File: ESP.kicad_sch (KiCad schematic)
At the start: 25 parts, among them J11 USB_C_Receptacle_USB2.0_16P, J12 UART_Breakout, U1 TLV1117LV33DCYR, U3 ESP32-C6-MINI-1/U

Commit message: is it time to give up :3
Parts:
- removed D6, D7: TVS, Diode_SMD:D_0603_1608Metric, symbol Device:D_TVS
- added D5: PRTR5V0U2AX,215, tv diode:PRTR5V0U2X, symbol tvs diode:PRTR5V0U2AX,215
- C10: renamed from C9; footprint Capacitor_SMD:C_0603_1608Metric -> Capacitor_SMD:C_0805_2012Metric
- C11: renamed from C10; footprint Capacitor_SMD:C_0603_1608Metric -> Capacitor_SMD:C_0805_2012Metric
- C4: renamed from C3; footprint Capacitor_SMD:C_0603_1608Metric -> Capacitor_SMD:C_0805_2012Metric
- C5: renamed from C4; footprint Capacitor_SMD:C_0603_1608Metric -> Capacitor_SMD:C_0805_2012Metric
- C6: renamed from C5; footprint Capacitor_SMD:C_0603_1608Metric -> Capacitor_SMD:C_0805_2012Metric
- C8: renamed from C7; footprint Capacitor_SMD:C_0603_1608Metric -> Capacitor_SMD:C_0805_2012Metric
- D2, D3: footprint LED_SMD:LED_0603_1608Metric -> LED_SMD:LED_0805_2012Metric
- renumbered C6 to C7, C8 to C9, D5 to D6, J11 to J10, J12 to J11
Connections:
- net BOOT: now also U3.24 (GPIO18); no longer U3.23 (GPIO9)
- net GND: now also D5.1 (GND)
- net LED3: now also U3.23 (GPIO9); no longer U3.24 (GPIO18)
- net USB_D+: now also D5.3 (IO2)
- net USB_D-: now also D5.2 (IO1)
- net VBUSB: now also D5.4 (VIN)
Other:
- moved on the sheet: C11, D6, R13, R14

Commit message: minor fixes
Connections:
- net BOOT: now also U3.25 (GPIO19); no longer U3.24 (GPIO18)
- net LED4: now also U3.24 (GPIO18); no longer U3.25 (GPIO19)
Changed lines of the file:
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@@
 		)
 	)
+	(label "BOOT"
+		(at 213.36 76.2 180)
+		(effects
+			(font
+				(size 1.27 1.27)
+			)
+			(justify right bottom)
+		)
+	)
 	(label "3V3_USB"
 		(at 41.91 43.18 0)
@@
 		)
 	)
-	(label "3V3"
-		(at 118.11 43.18 180)
+	(label "LED4"
+		(at 213.36 73.66 180)
 		(effects
 			(font
@@
 		)
 	)
-	(label "LED4"
-		(at 213.36 76.2 180)
+	(label "3V3"
+		(at 118.11 43.18 180)
 		(effects
 			(font
@@
 		)
 	)
-	(label "BOOT"
-		(at 213.36 73.66 180)
-		(effects
-			(font
-				(size 1.27 1.27)
-			)
-			(justify right bottom)
-		)
-	)
 	(label "IO6"
 		(at 281.305 71.755 180)
@@
 		(dnp no)
 		(fields_autoplaced yes)
-		(property "Reference" "#PWR044"
+		(property "Reference" "#PWR043"
 			(at 175.26 104.14 0)
 			(effects
@@
 			(project ""
 				(path "/795c8e51-3ded-4d21-b864-aaff31c5def7/6282503b-e4ab-454b-a074-f701a067f39b"
-					(reference "#PWR044")
+					(reference "#PWR043")
 					(unit 1)
 				)
@@
 			)
 		)
-		(property "Datasheet" ""
+		(property "Datasheet" "https://www.ti.com/lit/ds/symlink/lm66200.pdf?ts=1749979530840&ref_url=https%253A%252F%252Fwww.ti.com%252Fproduct%252FLM66200%253Futm_source%253Dgoogle%2526utm_medium%253Dcpc%2526utm_campaign%253Dapp-psil-null-44700045336317533_prodfolderdynamic-cpc-pf-google-eu_en_int%2526utm_content%253Dprodfolddynamic%2526ds_k%253DDYNAMIC+SEARCH+ADS%2526DCM%253Dyes%2526gad_source%253D1%2526gad_campaignid%253D8846228537%2526gbraid%253D0AAAAAC068F1nk_tvmYl3HXqK31USHPiW6%2526gclid%253DCjwKCAjw3rnCBhBxEiwArN0QE3nkB2-V_-iCZj5EyJCU-GAaAYaAjT6NO-eVHse-p8kje0rPcw2oyxoCwP4QAvD_BwE%2526gclsrc%253Daw.ds"
 			(at 77.47 44.45 0)
 			(effects
@@
 		(dnp no)
 		(fields_autoplaced yes)
-		(property "Reference" "#PWR043"
+		(property "Reference" "#PWR044"
 			(at 178.435 165.735 0)
 			(effects
@@
 			(project "VehicleControlUnit"
 				(path "/795c8e51-3ded-4d21-b864-aaff31c5def7/6282503b-e4ab-454b-a074-f701a067f39b"
-					(reference "#PWR043")
+					(reference "#PWR044")
 					(unit 1)
 				)
@@
 			)
 		)
-		(property "Datasheet" "~"
+		(property "Datasheet" "https://www.mouser.com/datasheet/2/80/CPDxx5V0R_HF_Series_RevC661473-2505247.pdf"
 			(at 201.295 146.05 0)
 			(effects

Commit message: 24v changes
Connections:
- net BOOT: now also U3.24 (GPIO18); no longer U3.25 (GPIO19)
- net LED3: now also U3.22 (GPIO8); no longer U3.23 (GPIO9)
- net LED4: now also U3.23 (GPIO9); no longer U3.24 (GPIO18)
- no-connect marks 3 -> 2
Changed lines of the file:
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@@
-	)
-	(no_connect
-		(at 203.2 63.5)
 	)
 	(no_connect
@@
 	(wire
 		(pts
+			(xy 203.2 66.04) (xy 213.36 66.04)
+		)
+		(stroke
+			(width 0)
+			(type default)
+		)
+	)
+	(wire
+		(pts
 			(xy 93.98 43.18) (xy 106.68 43.18)
 		)
@@
 	(wire
 		(pts
-			(xy 203.2 66.04) (xy 213.36 66.04)
-		)
-		(stroke
-			(width 0)
-			(type default)
-		)
-	)
-	(wire
-		(pts
 			(xy 213.36 45.72) (xy 219.71 45.72)
 		)
@@
 	(wire
 		(pts
+			(xy 203.2 73.66) (xy 213.36 73.66)
+		)
+		(stroke
+			(width 0)
+			(type default)
+		)
+	)
+	(wire
+		(pts
 			(xy 116.84 167.64) (xy 116.84 170.18)
 		)
@@
 	(wire
 		(pts
-			(xy 203.2 73.66) (xy 213.36 73.66)
-		)
-		(stroke
-			(width 0)
-			(type default)
-		)
-	)
-	(wire
-		(pts
 			(xy 203.2 43.18) (xy 210.82 43.18)
 		)
@@
 	(wire
 		(pts
+			(xy 203.2 63.5) (xy 213.36 63.5)
+		)
+		(stroke
+			(width 0)
+			(type default)
+		)
+	)
+	(wire
+		(pts
 			(xy 142.24 149.86) (xy 151.13 149.86)
 		)
@@
 		(pts
 			(xy 139.7 149.86) (xy 142.24 149.86)
-		)
-		(stroke
-			(width 0)
-			(type default)
-		)
-	)
-	(wire
-		(pts
-			(xy 203.2 76.2) (xy 213.36 76.2)
 		)
 		(stroke
@@
 		)
 	)
-	(label "LED3"
-		(at 213.36 66.04 180)
-		(effects
-			(font
-				(size 1.27 1.27)
-			)
-			(justify right bottom)
-		)
-	)
 	(label "IO3"
 		(at 230.505 88.265 0)
@@
 		)
 	)
-	(label "BOOT"
-		(at 213.36 76.2 180)
-		(effects
-			(font
-				(size 1.27 1.27)
-			)
-			(justify right bottom)
-		)
-	)
 	(label "3V3_USB"
 		(at 41.91 43.18 0)
@@
 		)
 	)
+	(label "LED4"
+		(at 213.36 66.04 180)
+		(effects
+			(font
+				(size 1.27 1.27)
+			)
+			(justify right bottom)
+		)
+	)
 	(label "3V3"
 		(at 175.26 26.67 270)
@@
 		)
 	)
+	(label "LED3"
+		(at 213.36 63.5 180)
+		(effects
+			(font
+				(size 1.27 1.27)
+			)
+			(justify right bottom)
+		)
+	)
 	(label "LED1"
 		(at 213.36 68.58 180)
@@
 		)
 	)
-	(label "LED4"
-		(at 213.36 73.66 180)
-		(effects
-			(font
-				(size 1.27 1.27)
-			)
-			(justify right bottom)
-		)
-	)
 	(label "3V3"
 		(at 118.11 43.18 180)
@@
 		(effects
 			(font
+				(size 1.27 1.27)
+			)
+			(justify right bottom)
+		)
+	)
+	(label "BOOT"
+		(at 213.36 73.66 180)
+		(effects
+			(font

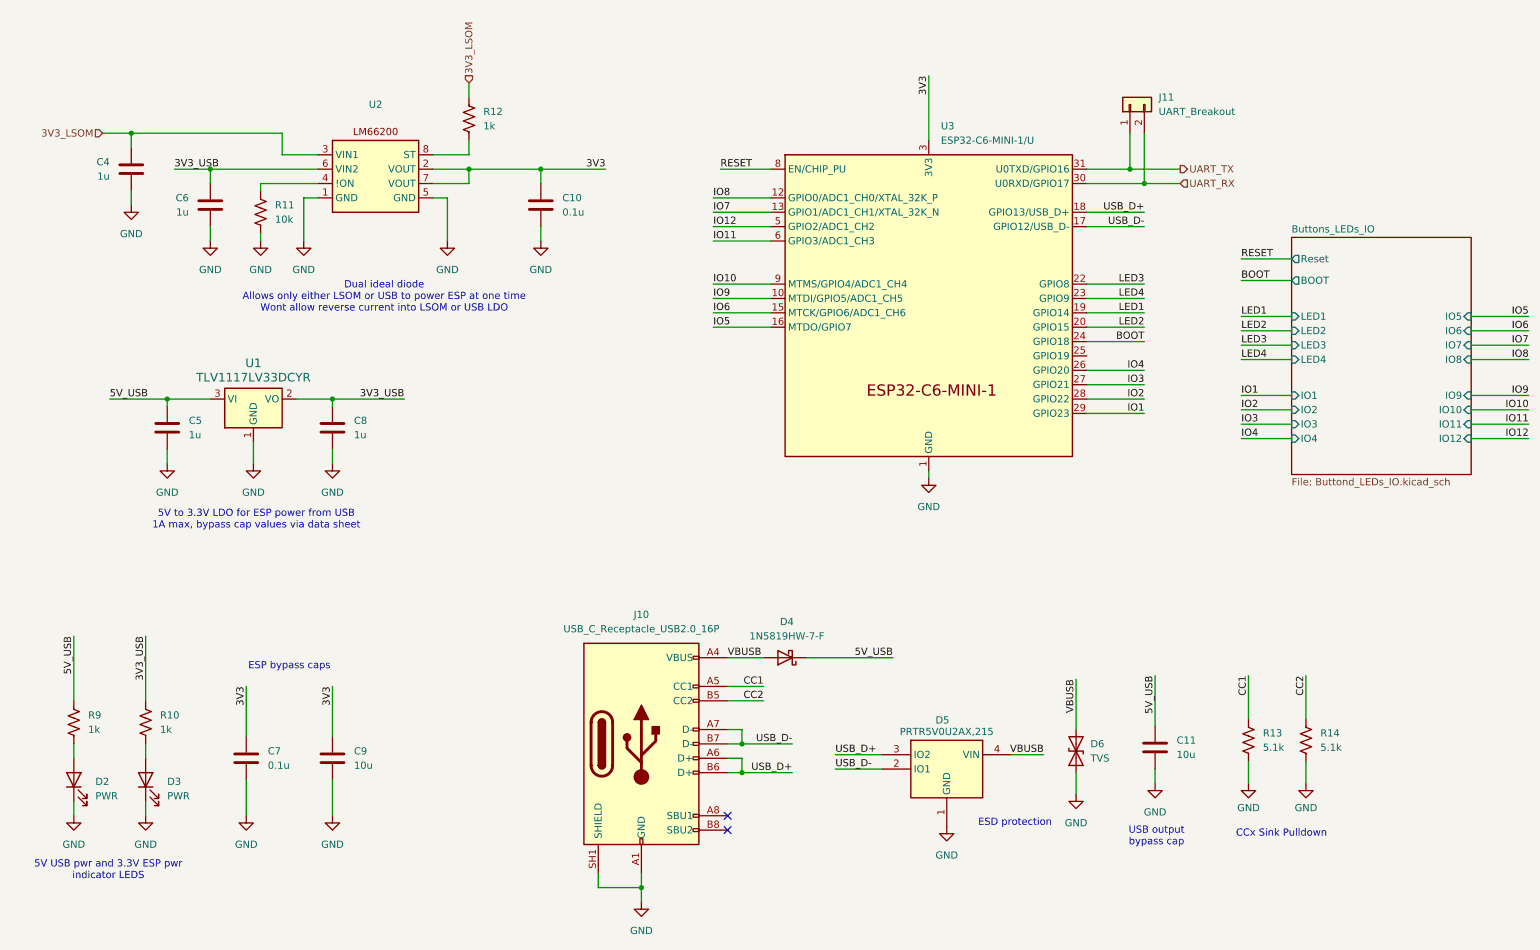
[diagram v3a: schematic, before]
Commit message: moving to kicad-bild
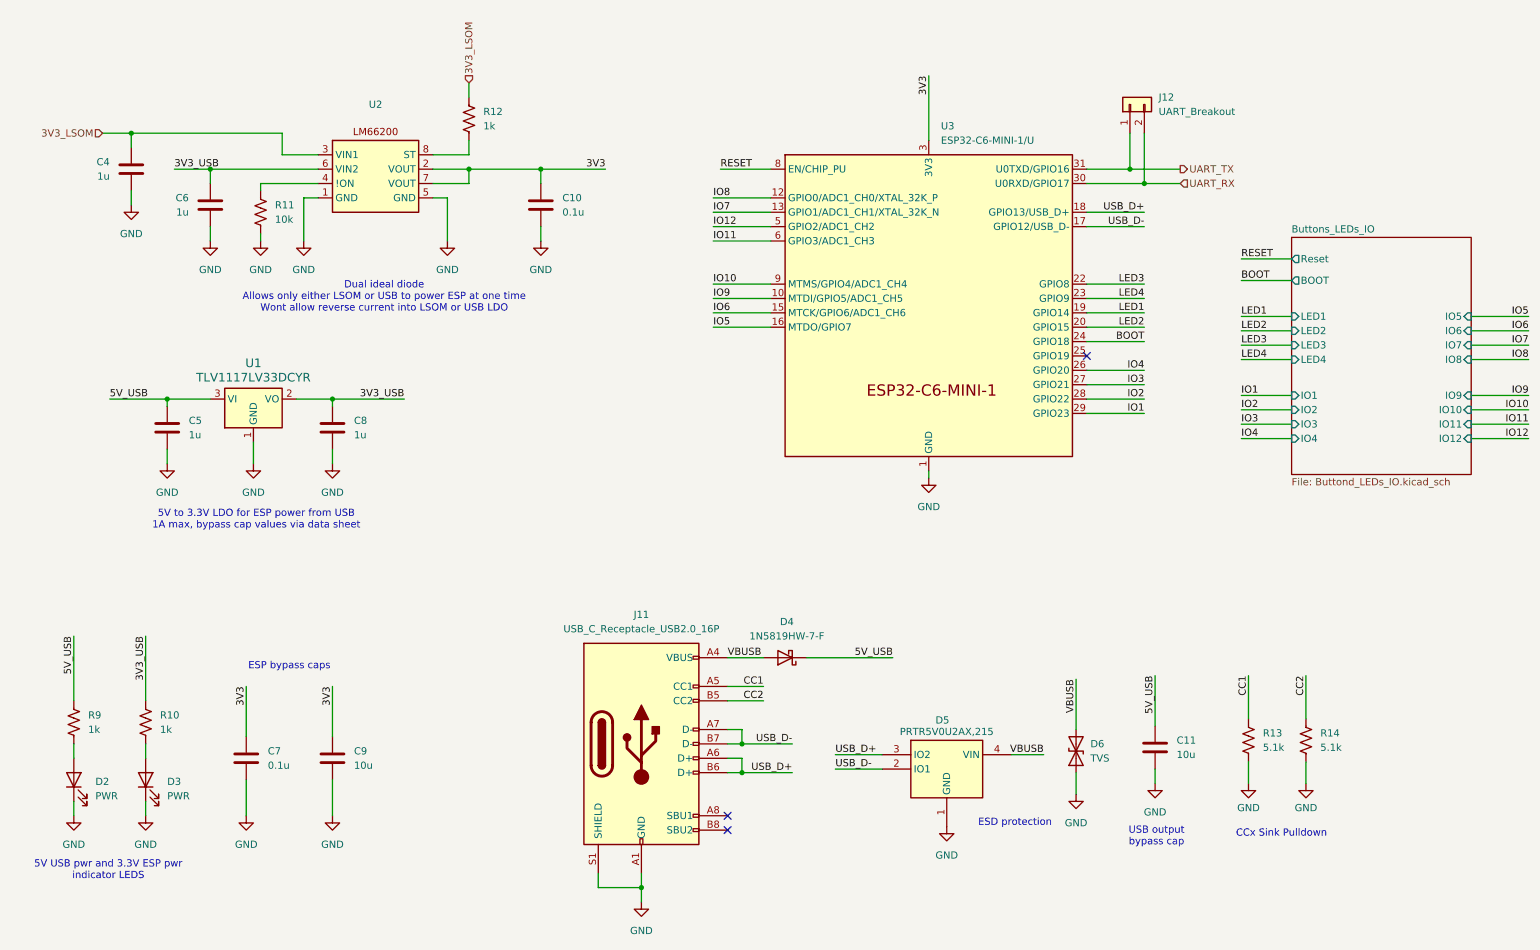
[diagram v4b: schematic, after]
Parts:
- renumbered J10 to J11, J11 to J12
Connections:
- net GND: now also J11.S1 (SHIELD); no longer J11.SH1 (SHIELD), J11.SH2 (SHIELD), J11.SH3 (SHIELD), J11.SH4 (SHIELD)
- no-connect marks 2 -> 3
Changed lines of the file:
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@@
 	)
 	(no_connect
+		(at 203.2 76.2)
+	)
+	(no_connect
 		(at 139.7 160.02)
 	)
@@
 		(dnp no)
 		(fields_autoplaced yes)
-		(property "Reference" "#PWR032"
+		(property "Reference" "#PWR034"
 			(at 40.64 101.6 0)
 			(effects
@@
 			(project "VehicleControlUnit"
 				(path "/795c8e51-3ded-4d21-b864-aaff31c5def7/6282503b-e4ab-454b-a074-f701a067f39b"
-					(reference "#PWR032")
+					(reference "#PWR034")
 					(unit 1)
 				)
@@
 		(on_board yes)
 		(dnp no)
-		(property "Reference" "#PWR047"
+		(property "Reference" "#PWR049"
 			(at 231.775 158.115 0)
 			(effects
@@
 			(project "VehicleControlUnit"
 				(path "/795c8e51-3ded-4d21-b864-aaff31c5def7/6282503b-e4ab-454b-a074-f701a067f39b"
-					(reference "#PWR047")
+					(reference "#PWR049")
 					(unit 1)
 				)
@@
 		(dnp no)
 		(fields_autoplaced yes)
-		(property "Reference" "#PWR037"
+		(property "Reference" "#PWR039"
 			(at 64.77 62.23 0)
 			(effects
@@
 			(project "VehicleControlUnit"
 				(path "/795c8e51-3ded-4d21-b864-aaff31c5def7/6282503b-e4ab-454b-a074-f701a067f39b"
-					(reference "#PWR037")
+					(reference "#PWR039")
 					(unit 1)
 				)
@@
 		(dnp no)
 		(fields_autoplaced yes)
-		(property "Reference" "#PWR038"
+		(property "Reference" "#PWR040"
 			(at 69.85 101.6 0)
 			(effects
@@
 			(project "VehicleControlUnit"
 				(path "/795c8e51-3ded-4d21-b864-aaff31c5def7/6282503b-e4ab-454b-a074-f701a067f39b"
-					(reference "#PWR038")
+					(reference "#PWR040")
 					(unit 1)
 				)
@@
 		(dnp no)
 		(fields_autoplaced yes)
-		(property "Reference" "#PWR031"
+		(property "Reference" "#PWR033"
 			(at 36.83 163.83 0)
 			(effects
@@
 			(project "VehicleControlUnit"
 				(path "/795c8e51-3ded-4d21-b864-aaff31c5def7/6282503b-e4ab-454b-a074-f701a067f39b"
-					(reference "#PWR031")
+					(reference "#PWR033")
 					(unit 1)
 				)
@@
 		(dnp no)
 		(fields_autoplaced yes)
-		(property "Reference" "#PWR033"
+		(property "Reference" "#PWR035"
 			(at 48.26 62.23 0)
 			(effects
@@
 			(project "VehicleControlUnit"
 				(path "/795c8e51-3ded-4d21-b864-aaff31c5def7/6282503b-e4ab-454b-a074-f701a067f39b"
-					(reference "#PWR033")
+					(reference "#PWR035")
 					(unit 1)
 				)
@@
 		(dnp no)
 		(fields_autoplaced yes)
-		(property "Reference" "J11"
+		(property "Reference" "J12"
 			(at 215.9 30.4799 90)
 			(effects
@@
 			(project ""
 				(path "/795c8e51-3ded-4d21-b864-aaff31c5def7/6282503b-e4ab-454b-a074-f701a067f39b"
-					(reference "J11")
+					(reference "J12")
 					(unit 1)
 				)
@@
 		(dnp no)
 		(fields_autoplaced yes)
-		(property "Reference" "#PWR043"
+		(property "Reference" "#PWR045"
 			(at 175.26 104.14 0)
 			(effects
@@
 			(project ""
 				(path "/795c8e51-3ded-4d21-b864-aaff31c5def7/6282503b-e4ab-454b-a074-f701a067f39b"
-					(reference "#PWR043")
+					(reference "#PWR045")
 					(unit 1)
 				)
@@
 		(dnp no)
 		(fields_autoplaced yes)
-		(property "Reference" "#PWR042"
+		(property "Reference" "#PWR044"
 			(at 124.46 179.07 0)
 			(effects
@@
 			(project "VehicleControlUnit"
 				(path "/795c8e51-3ded-4d21-b864-aaff31c5def7/6282503b-e4ab-454b-a074-f701a067f39b"
-					(reference "#PWR042")
+					(reference "#PWR044")
 					(unit 1)
 				)
@@
 			)
 		)
-		(property "Datasheet" "https://www.diodes.com/assets/Datasheets/1N5819HW.pdf"
+		(property "Datasheet" "~"
 			(at 149.86 129.54 0)
 			(effects
@@
 			)
 		)
+		(property "Sim.Pins" "1=K 2=A"
+			(at 36.83 151.13 0)
+			(effects
+				(font
+					(size 1.27 1.27)
+				)
+				(hide yes)
+			)
+		)
 		(pin "2"
 		)
@@
 		(dnp no)
 		(fields_autoplaced yes)
-		(property "Reference" "#PWR046"
+		(property "Reference" "#PWR048"
 			(at 215.265 158.115 0)
 			(effects
@@
 			(project "VehicleControlUnit"
 				(path "/795c8e51-3ded-4d21-b864-aaff31c5def7/6282503b-e4ab-454b-a074-f701a067f39b"
-					(reference "#PWR046")
+					(reference "#PWR048")
 					(unit 1)
 				)
@@
 			)
 		)
+		(property "Sim.Pins" "1=K 2=A"
+			(at 24.13 151.13 0)
+			(effects
+				(font
+					(size 1.27 1.27)
+				)
+				(hide yes)
+			)
+		)
 		(pin "2"
 		)
@@
 		(dnp no)
 		(fields_autoplaced yes)
-		(property "Reference" "J10"
+		(property "Reference" "J11"
 			(at 124.46 121.92 0)
 			(effects
@@
 			)
 		)
-		(property "Datasheet" "https://www.mouser.com/datasheet/2/837/usb4215-3472997.pdf"
+		(property "Datasheet" "https://www.usb.org/sites/default/files/documents/usb_type-c.zip"
 			(at 128.27 144.78 0)
 			(effects
@@
 		(pin "A1"
 		)
-		(pin "SH3"
-		)
 		(pin "B12"
 		)
@@
 		(pin "A8"
 		)
-		(pin "SH4"
-		)
-		(pin "SH2"
-		)
-		(pin "SH1"
+		(pin "S1"
 		)
 		(instances
 			(project "VehicleControlUnit"
 				(path "/795c8e51-3ded-4d21-b864-aaff31c5def7/6282503b-e4ab-454b-a074-f701a067f39b"
-					(reference "J10")
+					(reference "J11")
 					(unit 1)
 				)
@@
 		(dnp no)
 		(fields_autoplaced yes)
-		(property "Reference" "#PWR029"
+		(property "Reference" "#PWR031"
 			(at 24.13 163.83 0)
 			(effects
@@
 			(project "VehicleControlUnit"
 				(path "/795c8e51-3ded-4d21-b864-aaff31c5def7/6282503b-e4ab-454b-a074-f701a067f39b"
-					(reference "#PWR029")
+					(reference "#PWR031")
 					(unit 1)
 				)
@@
 		(dnp no)
 		(fields_autoplaced yes)
-		(property "Reference" "#PWR036"
+		(property "Reference" "#PWR038"
 			(at 57.15 62.23 0)
 			(effects
@@
 			(project "VehicleControlUnit"
 				(path "/795c8e51-3ded-4d21-b864-aaff31c5def7/6282503b-e4ab-454b-a074-f701a067f39b"
-					(reference "#PWR036")
+					(reference "#PWR038")
 					(unit 1)
 				)
@@
 		(dnp no)
 		(fields_autoplaced yes)
-		(property "Reference" "#PWR041"
+		(property "Reference" "#PWR043"
 			(at 106.68 62.23 0)
 			(effects
@@
 			(project "VehicleControlUnit"
 				(path "/795c8e51-3ded-4d21-b864-aaff31c5def7/6282503b-e4ab-454b-a074-f701a067f39b"
-					(reference "#PWR041")
+					(reference "#PWR043")
 					(unit 1)
 				)
@@
 	)
 	(symbol
-		(lib_name "R_US_1")
 		(lib_id "Device:R_US")
 		(at 231.775 144.145 0)
@@
 		(dnp no)
 		(fields_autoplaced yes)
-		(property "Reference" "#PWR035"
+		(property "Reference" "#PWR037"
 			(at 55.88 101.6 0)
 			(effects
@@
 			(project "VehicleControlUnit"
 				(path "/795c8e51-3ded-4d21-b864-aaff31c5def7/6282503b-e4ab-454b-a074-f701a067f39b"
-					(reference "#PWR035")
+					(reference "#PWR037")
 					(unit 1)
 				)
@@
 		(dnp no)
 		(fields_autoplaced yes)
-		(property "Reference" "#PWR045"
+		(property "Reference" "#PWR047"
 			(at 201.295 160.02 0)
 			(effects
@@
 			(project "VehicleControlUnit"
 				(path "/795c8e51-3ded-4d21-b864-aaff31c5def7/6282503b-e4ab-454b-a074-f701a067f39b"
-					(reference "#PWR045")
+					(reference "#PWR047")
 					(unit 1)
 				)
@@
 		(dnp no)
 		(fields_autoplaced yes)
-		(property "Reference" "#PWR039"
+		(property "Reference" "#PWR041"
 			(at 69.85 163.83 0)
 			(effects
@@
 			(project "VehicleControlUnit"
 				(path "/795c8e51-3ded-4d21-b864-aaff31c5def7/6282503b-e4ab-454b-a074-f701a067f39b"
-					(reference "#PWR039")
+					(reference "#PWR041")
 					(unit 1)
 				)
@@
 		(on_board yes)
 		(dnp no)
-		(property "Reference" "#PWR048"
+		(property "Reference" "#PWR050"
 			(at 241.935 158.115 0)
 			(effects
@@
 			(project "VehicleControlUnit"
 				(path "/795c8e51-3ded-4d21-b864-aaff31c5def7/6282503b-e4ab-454b-a074-f701a067f39b"
-					(reference "#PWR048")
+					(reference "#PWR050")
 					(unit 1)
 				)
@@
 		(dnp no)
 		(fields_autoplaced yes)
-		(property "Reference" "#PWR030"
+		(property "Reference" "#PWR032"
 			(at 34.29 55.88 0)
 			(effects
@@
 			(project "VehicleControlUnit"
 				(path "/795c8e51-3ded-4d21-b864-aaff31c5def7/6282503b-e4ab-454b-a074-f701a067f39b"
-					(reference "#PWR030")
+					(reference "#PWR032")
 					(unit 1)
 				)
@@
 		(dnp no)
 		(fields_autoplaced yes)
-		(property "Reference" "#PWR044"
+		(property "Reference" "#PWR046"
 			(at 178.435 165.735 0)
 			(effects
@@
 			(project "VehicleControlUnit"
 				(path "/795c8e51-3ded-4d21-b864-aaff31c5def7/6282503b-e4ab-454b-a074-f701a067f39b"
-					(reference "#PWR044")
+					(reference "#PWR046")
 					(unit 1)
 				)
@@
 		(dnp no)
 		(fields_autoplaced yes)
-		(property "Reference" "#PWR040"
+		(property "Reference" "#PWR042"
 			(at 90.17 62.23 0)
 			(effects
@@
 			(project "VehicleControlUnit"
 				(path "/795c8e51-3ded-4d21-b864-aaff31c5def7/6282503b-e4ab-454b-a074-f701a067f39b"
-					(reference "#PWR040")
+					(reference "#PWR042")
 					(unit 1)
 				)
@@
 		(dnp no)
 		(fields_autoplaced yes)
-		(property "Reference" "#PWR034"
+		(property "Reference" "#PWR036"
 			(at 54.61 163.83 0)
 			(effects
@@
 			(project "VehicleControlUnit"
 				(path "/795c8e51-3ded-4d21-b864-aaff31c5def7/6282503b-e4ab-454b-a074-f701a067f39b"
-					(reference "#PWR034")
+					(reference "#PWR036")
 					(unit 1)
 				)
@@
 	)
 	(symbol
-		(lib_name "R_US_2")
 		(lib_id "Device:R_US")
 		(at 241.935 144.145 0)
@@
 			)
 		)
-		(property "Datasheet" "https://www.mouser.com/datasheet/2/80/CPDxx5V0R_HF_Series_RevC661473-2505247.pdf"
+		(property "Datasheet" "~"
 			(at 201.295 146.05 0)
 			(effects

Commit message: fuck the rats nest im doing it tomorrow
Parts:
- removed J12: UART_Breakout, Connector_PinHeader_2.54mm:PinHeader_1x02_P2.54mm_Vertical, symbol Connector_Generic:Conn_01x02
- D5: footprint tv diode:PRTR5V0U2X -> UTSVT_Passives:PRTR5V0U2X
- J9: renamed from J11; footprint USBC:GCT_USB4215-03-A_REVA -> UTSVT_Connectors:GCT_USB4215-03-A_REVA
- U3: renamed from U2; footprint LM66200:SOTFL50P160X60-8N -> UTSVT_Power:SOTFL50P160X60-8N
- U4: renamed from U3; footprint ESP32-C6-MINI-1:ESP32-C6-MINI-1 -> UTSVT_Special:ESP32-C6-MINI-1; symbol PCM_Espressif:ESP32-C6-MINI-1/U -> utsvt_special:ESP32-C6-MINI-1/U
- renumbered C9 to C10, C10 to C11, C11 to C12, C4 to C5, C5 to C6, C6 to C7, C7 to C8, C8 to C9, R13 to R10, R14 to R11, R9 to R6, R10 to R7, R11 to R8, R12 to R9, U1 to U2
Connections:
- net IO13: now reaches U4.25 (GPIO19)
- no-connect marks 3 -> 2
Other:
- sheet Buttons_LEDs_IO ports: added IO13, USB_D+, USB_D-; removed none

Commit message: routing done
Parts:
- J9: footprint UTSVT_Connectors:GCT_USB4215-03-A_REVA -> UTSVT_ICs:USB_C_Receptacle_GCT_USB4105-xx-A_16P_TopMnt_Horizontal; symbol Connector:USB_C_Receptacle_USB2.0_16P -> UTSVT_Connectors:USB_C_Receptacle_USB2.0_16P
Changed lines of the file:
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@@
 	)
 	(symbol
-		(lib_id "Connector:USB_C_Receptacle_USB2.0_16P")
+		(lib_id "UTSVT_Connectors:USB_C_Receptacle_USB2.0_16P")
 		(at 124.46 144.78 0)
 		(unit 1)
@@
 			)
 		)
-		(property "Footprint" "UTSVT_Connectors:GCT_USB4215-03-A_REVA"
+		(property "Footprint" "UTSVT_ICs:USB_C_Receptacle_GCT_USB4105-xx-A_16P_TopMnt_Horizontal"
 			(at 128.27 144.78 0)
 			(effects
